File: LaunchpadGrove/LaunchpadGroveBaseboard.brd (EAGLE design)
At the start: 100 x 80 mm, 13 parts

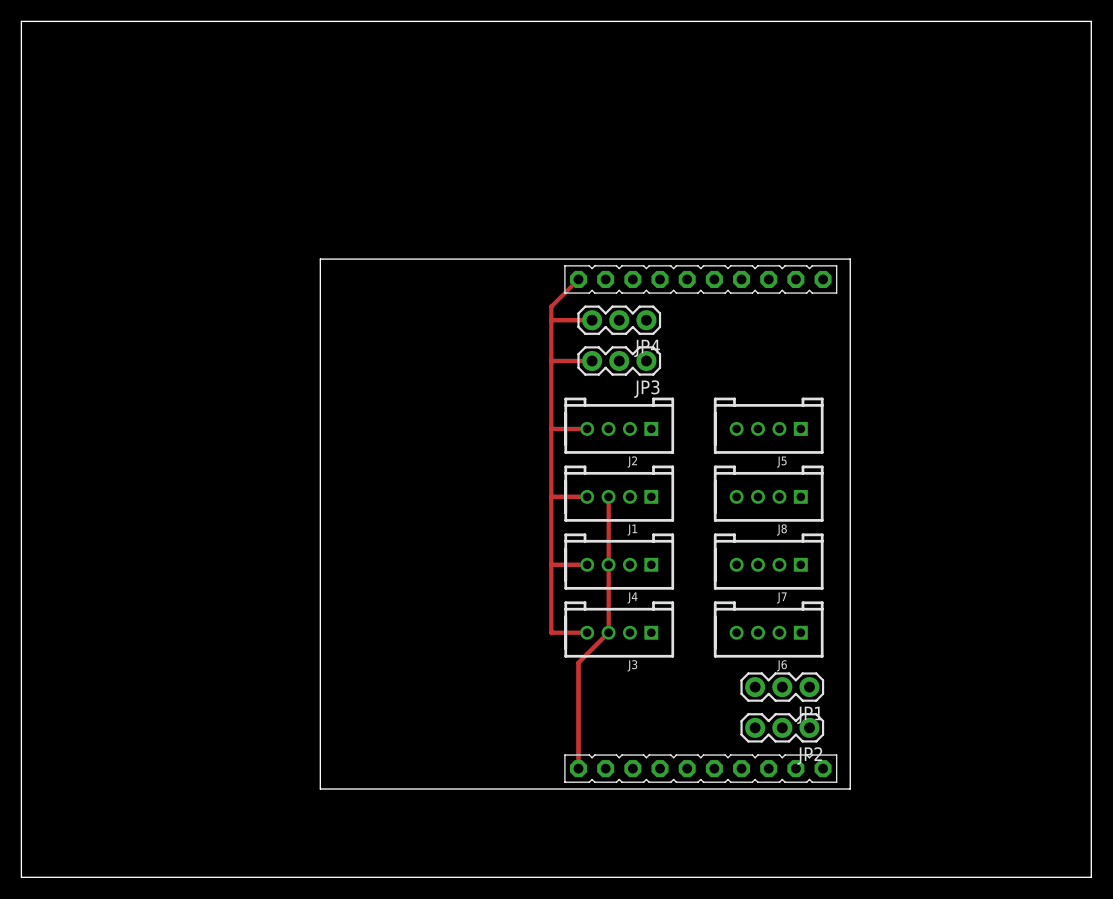
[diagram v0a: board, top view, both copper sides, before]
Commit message: Added switch, vbat, cct protection etc
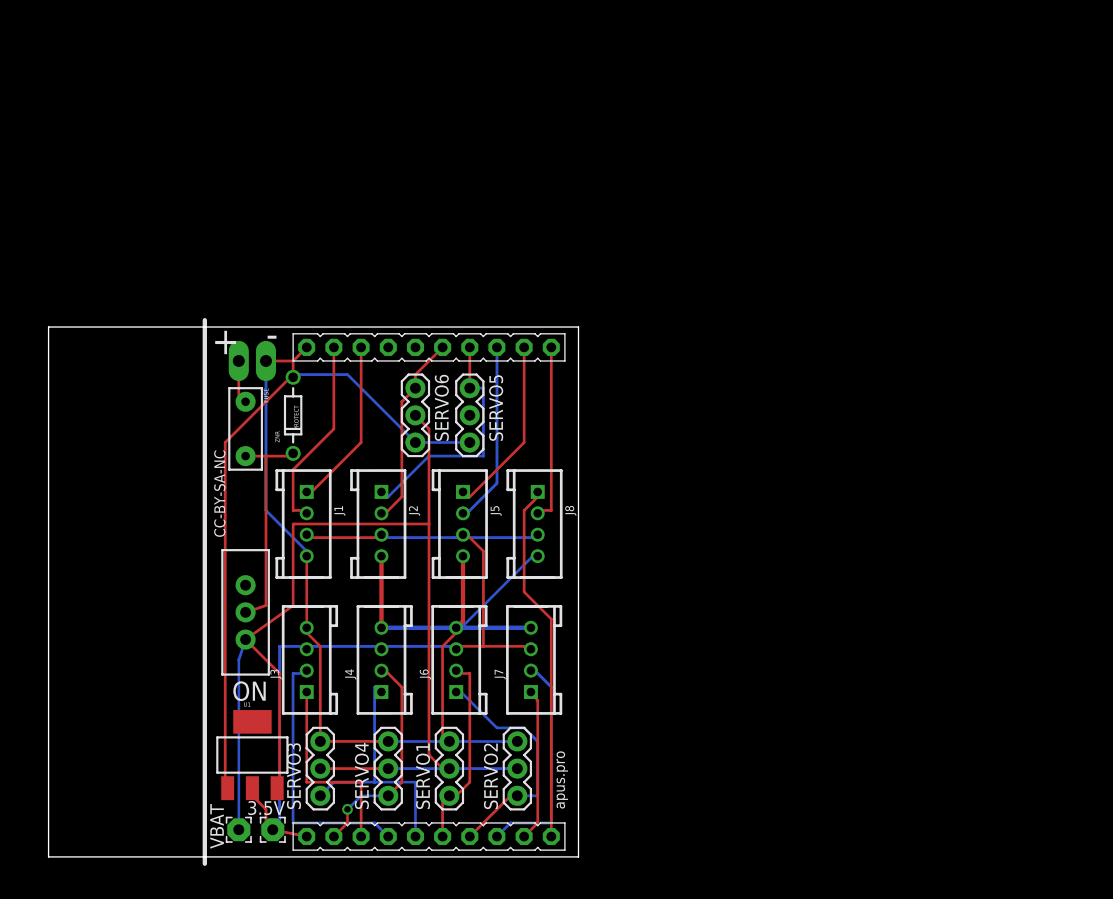
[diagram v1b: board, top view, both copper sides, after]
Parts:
- removed JP1, JP2, JP3, JP4: (no value), SparkFun:1X03
- added 3.5V, VBAT: (no value), wirepad:2,15/1,0
- added BAT: (no value), SparkFun:1X02_LONGPADS
- added FUSE: PTC, SparkFun:PTC
- added ON: (no value), SparkFun:SWITCH-SPDT
- added SERVO1, SERVO2, SERVO3, SERVO4, SERVO5, SERVO6: (no value), SparkFun:1X03
- added U1: V_REG_317SMD, SparkFun:SOT223
- added ZNR: PROTECT, SparkFun:DIODE-ZENER
- moved J5 29.9 mm to (41.3, 33.0), turned to 270 degrees
- moved J1 29.3 mm to (26.7, 33.0), turned to 270 degrees
- moved J3 29.3 mm to (26.7, 20.3), turned to 90 degrees
- moved J6 29.3 mm to (40.6, 20.3), turned to 90 degrees
- moved U$1 26.2 mm to (2.54, 1.27)
- moved J4 23.9 mm to (33.7, 20.3), turned to 90 degrees
- moved J2 23.9 mm to (33.7, 33.0), turned to 270 degrees
- moved J7 23.9 mm to (47.6, 20.3), turned to 90 degrees
- moved J8 21.7 mm to (48.3, 33.0), turned to 270 degrees
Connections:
- removed net N$5: J4.2, U$1.P1.2
- new net N$1: J3.2, U$1.P1.2
- new net N$16: FUSE.P$2, ON.2, ZNR.P$1
- new net N$2: BAT.2, FUSE.P$1
- new net VBAT: ON.1, SERVO1.2, SERVO2.2, SERVO3.2, SERVO4.2, SERVO6.2, U1.3, VBAT.1
- net GND: now also BAT.1, J5.4, J7.4, SERVO1.3, SERVO2.3, SERVO3.3, SERVO4.3, SERVO5.3, SERVO6.3, U1.1, ZNR.P$2; no longer JP1.3, JP2.3, JP3.3, JP4.3
- net N$11: now also SERVO6.1; no longer JP4.1
- net N$12: now also SERVO5.1; no longer JP3.1
- net N$3: now also J4.2, SERVO4.1; no longer J3.2
- net N$6: now also SERVO3.1
- net N$7: now also SERVO1.1; no longer JP1.1
- net N$8: now also SERVO2.1; no longer JP2.1
- net VCC: now also 3.5V.1, J2.3, U1.2; no longer JP1.2, JP2.2, JP3.2, JP4.2
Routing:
- net GND: track 55.1 -> 174.2 mm
- net VBAT: track 0.00 -> 112.0 mm
- net VCC: track 26.6 -> 86.1 mm
- net N$17: track 0.00 -> 33.8 mm
- net N$1: track 0.00 -> 24.9 mm
- net N$6: track 0.00 -> 24.2 mm
- net N$8: track 0.00 -> 23.2 mm
- net N$12: track 0.00 -> 22.7 mm
- net N$15: track 0.00 -> 20.8 mm
- net N$16: track 0.00 -> 20.7 mm
- net N$3: track 0.00 -> 20.6 mm, vias 0 -> 1
- net N$4: track 0.00 -> 19.0 mm
- net N$7: track 0.00 -> 18.6 mm
- net N$9: track 0.00 -> 18.4 mm
- net N$11: track 0.00 -> 18.0 mm
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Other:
- board size 100 x 80 mm -> 49.5 x 49.5 mm
- board text added: "+"
- board text added: "-"
- board text added: "CC-BY-SA-NC"
- board text added: "apus.pro"

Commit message: Space for larger zener
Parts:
- BAT: device SparkFun:1X02_LONGPADS -> SparkFun:1X02
- ZNR: device SparkFun:DIODE-ZENER -> diode:DO41-10
- moved BAT 1.80 mm to (21.6, 49.5)
- moved ZNR 1.80 mm to (24.1, 44.5)
- moved FUSE 1.27 mm to (19.7, 41.9)
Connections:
- net GND: now also ZNR.A; no longer ZNR.P$2
- net N$16: now also ZNR.C; no longer ZNR.P$1
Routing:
- net GND: track 174.2 -> 182.3 mm, vias 0 -> 1
- net N$2: track 4.44 -> 5.71 mm
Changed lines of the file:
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@@
 <plain>
 <wire x1="17.145" y1="1.27" x2="17.145" y2="52.07" width="0.4064" layer="21"/>
-<text x="17.78" y="48.895" size="2.54" layer="21">+</text>
-<text x="22.86" y="49.53" size="2.54" layer="21">-</text>
-<text x="19.05" y="31.75" size="1.016" layer="21" rot="R90">CC-BY-SA-NC</text>
+<text x="17.78" y="45.72" size="2.54" layer="21">+</text>
+<text x="22.86" y="46.355" size="2.54" layer="21">-</text>
+<text x="35.56" y="47.625" size="1.016" layer="21" rot="R180">CC-BY-SA-NC</text>
 <text x="50.8" y="6.35" size="1.016" layer="21" rot="R90">apus.pro</text>
 </plain>
@@
 <element name="SERVO4" library="SparkFun" package="1X03" value="" x="34.29" y="7.62" rot="R90"/>
 <element name="U1" library="SparkFun" package="SOT223" value="V_REG_317SMD" x="21.59" y="11.43"/>
-<element name="BAT" library="SparkFun" package="1X02_LONGPADS" value="" x="22.86" y="48.26" rot="R180"/>
+<element name="BAT" library="SparkFun" package="1X02" value="" x="21.59" y="49.53" rot="R180"/>
 <element name="ON" library="SparkFun" package="SWITCH-SPDT" value="" x="20.955" y="24.765" smashed="yes" rot="R180">
 <attribute name="NAME" x="19.685" y="16.51" size="1.778" layer="25" ratio="10"/>
 <attribute name="VALUE" x="24.765" y="34.29" size="1.778" layer="27" ratio="10" rot="R180"/>
 </element>
-<element name="ZNR" library="SparkFun" package="DIODE-ZENER" value="PROTECT" x="25.4" y="43.18" rot="R90"/>
+<element name="ZNR" library="diode" package="DO41-10" value="PROTECT" x="24.13" y="44.45" rot="R90"/>
 <element name="VBAT" library="wirepad" package="2,15/1,0" value="" x="20.32" y="4.445" smashed="yes" rot="R90">
 <attribute name="NAME" x="18.923" y="2.667" size="1.27" layer="25" ratio="10" rot="R90"/>
@@
 <attribute name="VALUE" x="23.495" y="5.445" size="0.0254" layer="27"/>
 </element>
-<element name="FUSE" library="SparkFun" package="PTC" value="PTC" x="20.955" y="41.91" rot="R270"/>
+<element name="FUSE" library="SparkFun" package="PTC" value="PTC" x="19.685" y="41.91" rot="R270"/>
 </elements>
 <signals>
@@
 <contactref element="J1" pad="2"/>
 <wire x1="25.4" y1="34.29" x2="26.67" y2="34.29" width="0.254" layer="1"/>
-<wire x1="25.4" y1="38.1" x2="25.4" y2="34.29" width="0.254" layer="1"/>
-<wire x1="29.21" y1="41.91" x2="25.4" y2="38.1" width="0.254" layer="1"/>
-<wire x1="29.21" y1="49.53" x2="29.21" y2="41.91" width="0.254" layer="1"/>
+<wire x1="25.4" y1="36.83" x2="25.4" y2="34.29" width="0.254" layer="1"/>
+<wire x1="29.21" y1="40.64" x2="25.4" y2="36.83" width="0.254" layer="1"/>
+<wire x1="29.21" y1="49.53" x2="29.21" y2="40.64" width="0.254" layer="1"/>
 <wire x1="26.67" y1="34.29" x2="26.67" y2="34.02" width="0.254" layer="1"/>
 </signal>
@@
 <contactref element="U1" pad="1"/>
 <contactref element="BAT" pad="1"/>
-<contactref element="ZNR" pad="P$2"/>
+<contactref element="ZNR" pad="A"/>
 <wire x1="26.67" y1="30.02" x2="26.67" y2="23.32" width="0.254" layer="1"/>
 <wire x1="26.67" y1="30.48" x2="26.67" y2="30.02" width="0.254" layer="1"/>
@@
 <wire x1="40.005" y1="12.7" x2="34.29" y2="12.7" width="0.254" layer="16"/>
 <wire x1="41.91" y1="40.64" x2="36.83" y2="40.64" width="0.254" layer="16"/>
-<wire x1="19.05" y1="40.64" x2="19.05" y2="8.89" width="0.254" layer="1"/>
-<wire x1="25.4" y1="46.99" x2="19.05" y2="40.64" width="0.254" layer="1"/>
-<wire x1="19.05" y1="8.89" x2="19.2786" y2="8.3312" width="0.254" layer="1"/>
-<wire x1="25.4" y1="48.26" x2="26.67" y2="49.53" width="0.254" layer="1"/>
-<wire x1="25.4" y1="46.99" x2="25.4" y2="48.26" width="0.254" layer="1"/>
-<wire x1="25.4" y1="46.99" x2="25.4" y2="46.736" width="0.254" layer="1"/>
-<wire x1="25.4" y1="48.26" x2="22.86" y2="48.26" width="0.254" layer="1"/>
-<wire x1="30.48" y1="46.99" x2="36.83" y2="40.64" width="0.254" layer="16"/>
-<wire x1="25.4" y1="46.99" x2="30.48" y2="46.99" width="0.254" layer="16"/>
-<wire x1="25.4" y1="46.99" x2="25.4" y2="46.736" width="0.254" layer="16"/>
-<wire x1="22.86" y1="34.29" x2="26.67" y2="30.48" width="0.254" layer="16"/>
-<wire x1="22.86" y1="48.26" x2="22.86" y2="34.29" width="0.254" layer="16"/>
-<wire x1="26.67" y1="30.48" x2="26.67" y2="30.02" width="0.254" layer="16"/>
 <wire x1="33.655" y1="23.32" x2="33.655" y2="30.02" width="0.4064" layer="1"/>
 <wire x1="41.275" y1="30.02" x2="41.275" y2="23.955" width="0.4064" layer="1"/>
@@
 <wire x1="47.625" y1="23.32" x2="40.64" y2="23.32" width="0.4064" layer="16"/>
 <wire x1="33.655" y1="23.32" x2="40.64" y2="23.32" width="0.4064" layer="16"/>
+<wire x1="39.37" y1="38.1" x2="41.91" y2="40.64" width="0.254" layer="1"/>
+<wire x1="39.37" y1="21.59" x2="39.37" y2="38.1" width="0.254" layer="1"/>
+<wire x1="24.13" y1="49.53" x2="26.67" y2="49.53" width="0.254" layer="1"/>
+<wire x1="19.05" y1="36.83" x2="19.05" y2="8.89" width="0.254" layer="1"/>
+<wire x1="21.59" y1="39.37" x2="19.05" y2="36.83" width="0.254" layer="1"/>
+<wire x1="21.59" y1="49.53" x2="21.59" y2="39.37" width="0.254" layer="1"/>
+<wire x1="19.05" y1="8.89" x2="19.2786" y2="8.3312" width="0.254" layer="1"/>
+<wire x1="21.59" y1="49.53" x2="24.13" y2="49.53" width="0.254" layer="1"/>
+<wire x1="39.37" y1="45.72" x2="39.37" y2="38.1" width="0.254" layer="1"/>
+<wire x1="36.83" y1="48.26" x2="39.37" y2="45.72" width="0.254" layer="16"/>
+<wire x1="27.94" y1="48.26" x2="36.83" y2="48.26" width="0.254" layer="16"/>
+<wire x1="26.67" y1="49.53" x2="27.94" y2="48.26" width="0.254" layer="16"/>
+<via x="39.37" y="45.72" extent="1-16" drill="0.6096"/>
 </signal>
 <signal name="VBAT">
@@
 <contactref element="BAT" pad="2"/>
 <contactref element="FUSE" pad="P$1"/>
-<wire x1="20.32" y1="48.26" x2="20.32" y2="44.45" width="0.254" layer="1"/>
-<wire x1="20.32" y1="44.45" x2="20.955" y2="44.45" width="0.254" layer="1"/>
+<wire x1="19.05" y1="49.53" x2="19.05" y2="44.45" width="0.254" layer="1"/>
+<wire x1="19.05" y1="44.45" x2="19.685" y2="44.45" width="0.254" layer="1"/>
 </signal>
 <signal name="N$16">
 <contactref element="FUSE" pad="P$2"/>
 <contactref element="ON" pad="2"/>
-<contactref element="ZNR" pad="P$1"/>
-<wire x1="20.955" y1="39.37" x2="22.86" y2="39.37" width="0.254" layer="1"/>
-<wire x1="22.86" y1="39.37" x2="25.4" y2="39.37" width="0.254" layer="1"/>
-<wire x1="25.4" y1="39.37" x2="25.4" y2="39.624" width="0.254" layer="1"/>
-<wire x1="22.86" y1="25.4" x2="20.955" y2="24.765" width="0.254" layer="1"/>
-<wire x1="22.86" y1="39.37" x2="22.86" y2="25.4" width="0.254" layer="1"/>
+<contactref element="ZNR" pad="C"/>
+<wire x1="19.685" y1="39.37" x2="24.13" y2="39.37" width="0.254" layer="16"/>
+<wire x1="24.13" y1="27.94" x2="20.955" y2="24.765" width="0.254" layer="1"/>
+<wire x1="24.13" y1="39.37" x2="24.13" y2="27.94" width="0.254" layer="1"/>
 </signal>
 </signals>
